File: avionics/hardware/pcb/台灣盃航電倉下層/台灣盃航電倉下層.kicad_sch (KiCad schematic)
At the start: 42 parts, among them J1 XT60, J2 XT60, J4 Pyro1, J5 Pyro2, Q1 NMOS, Q2 NMOS, U3 LM2596S-5, U4 LM2596S-5, U5 AMS1117-3.3, U6 AMS1117-3.3

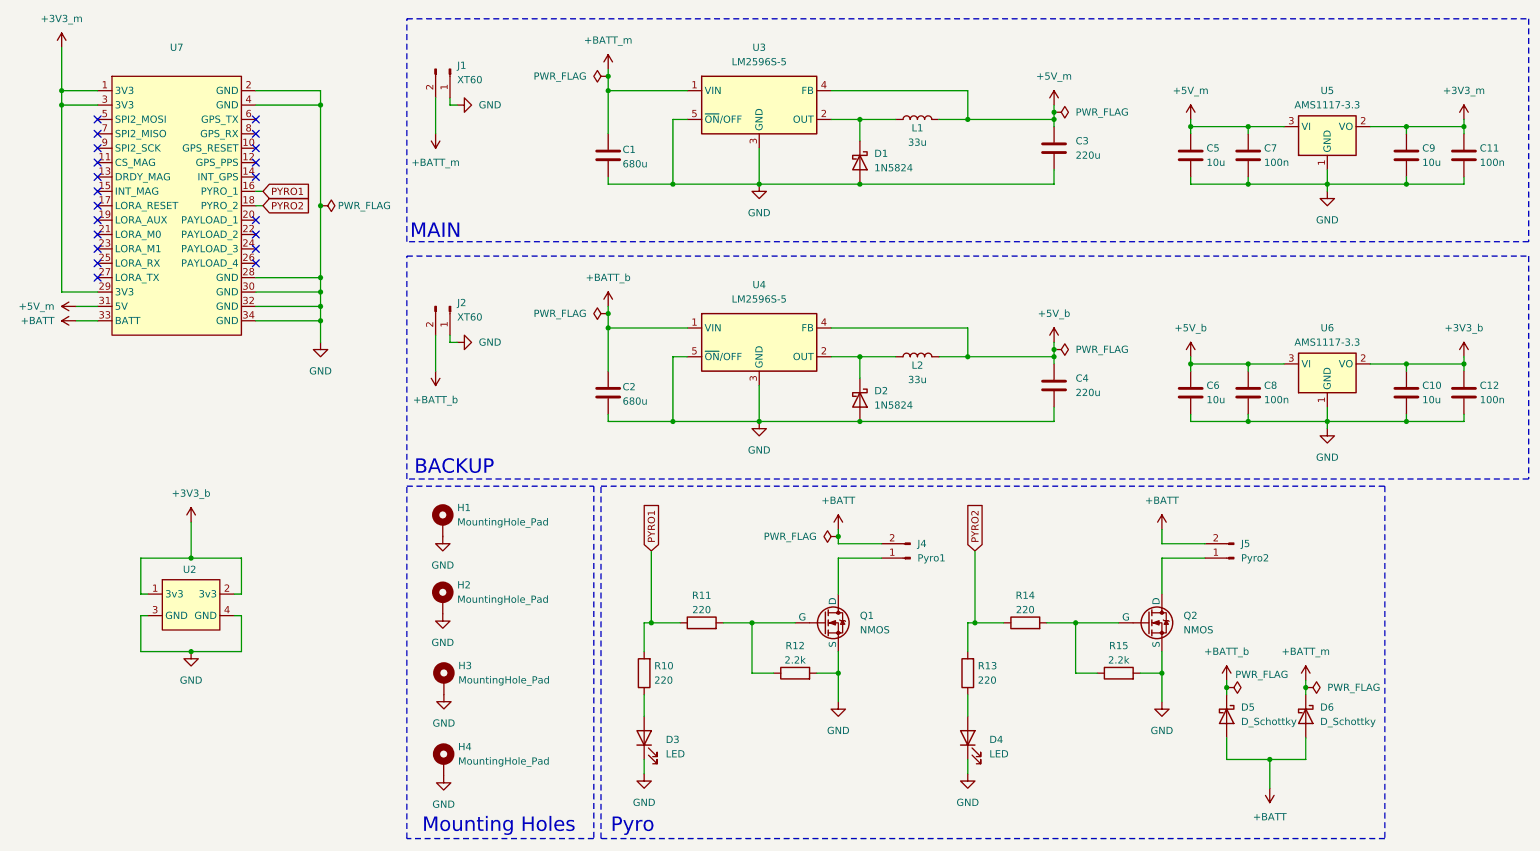
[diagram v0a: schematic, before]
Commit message: V1.2
change Schottky Diode to nmos
change the footprint of the 1n5824*2
change the circuit of the LM2596S-5*2
change the position of the igition*2
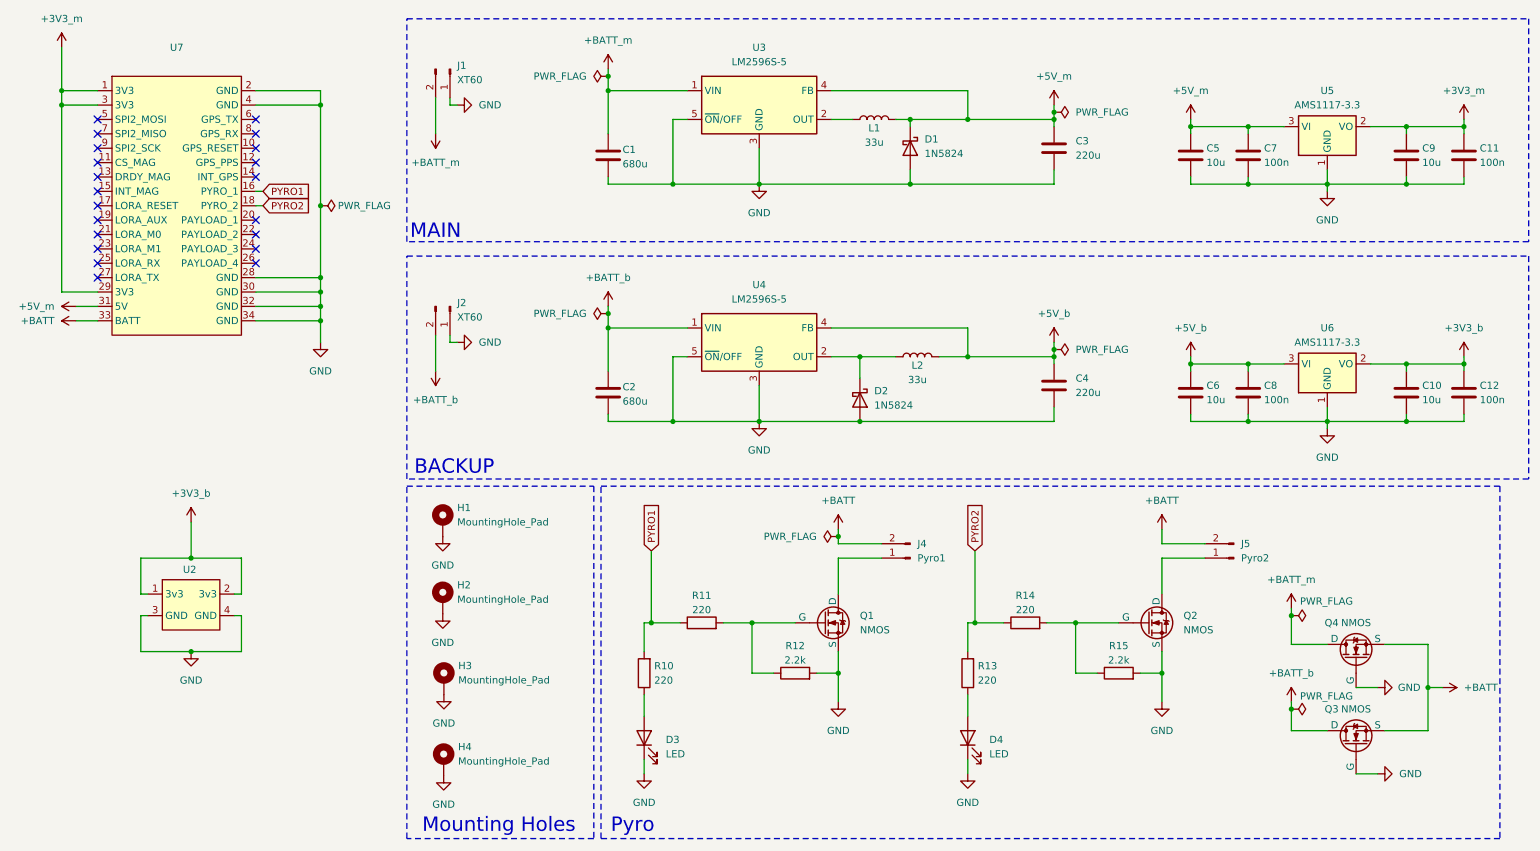
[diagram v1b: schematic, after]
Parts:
- removed D5, D6: D_Schottky, Diode_SMD:D_SMC, symbol Device:D_Schottky
- added Q3, Q4: NMOS, Package_TO_SOT_SMD:SOT-223, symbol Simulation_SPICE:NMOS
- D1, D2: footprint Diode_THT:D_DO-201AD_P15.24mm_Horizontal -> Diode_SMD:D_SMC
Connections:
- net +5V_m: now also D1.1 (K)
- net +BATT: now also Q3.3 (S), Q4.3 (S)
- net +BATT_b: now also Q3.1 (D)
- net +BATT_m: now also Q4.1 (D)
- net GND: now also Q3.2 (G), Q4.2 (G)
- net at L1.1, U3.2 (OUT): no longer D1.1 (K)
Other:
- moved on the sheet: D1, L1

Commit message: 完成所有航電板設計
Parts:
- U2: footprint Connector_PinHeader_2.54mm:PinHeader_2x02_P2.54mm_Vertical -> Connector_PinHeader_1.00mm:PinHeader_2x02_P1.00mm_Vertical
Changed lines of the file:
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@@
 			)
 		)
-		(property "Footprint" "Connector_PinHeader_2.54mm:PinHeader_2x02_P2.54mm_Vertical"
+		(property "Footprint" "Connector_PinHeader_1.00mm:PinHeader_2x02_P1.00mm_Vertical"
 			(at 46.99 113.03 0)
 			(effects
